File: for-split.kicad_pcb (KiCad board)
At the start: 2 copper layers, 114.3 x 95.3 mm, 84 parts, among them J1 TRRS, J2 TRRS, U1 ProMicro

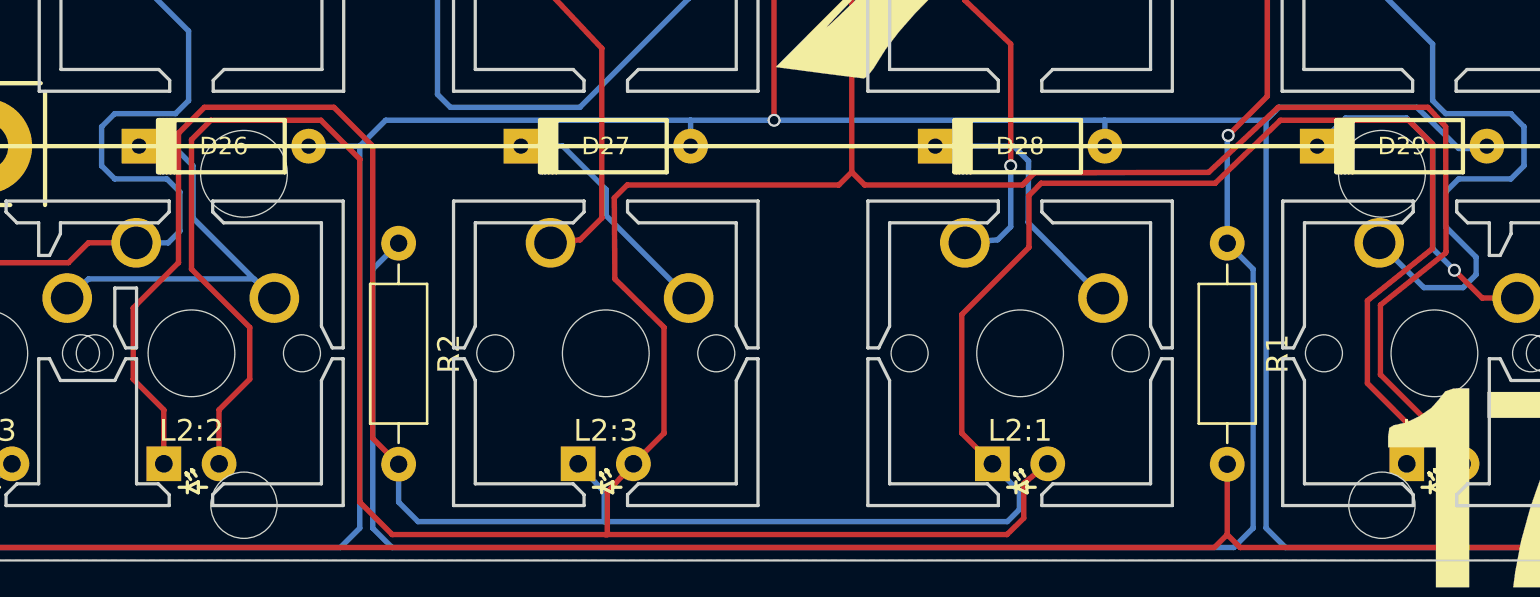
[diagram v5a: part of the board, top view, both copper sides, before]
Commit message: Fix L2.2 cathode trace
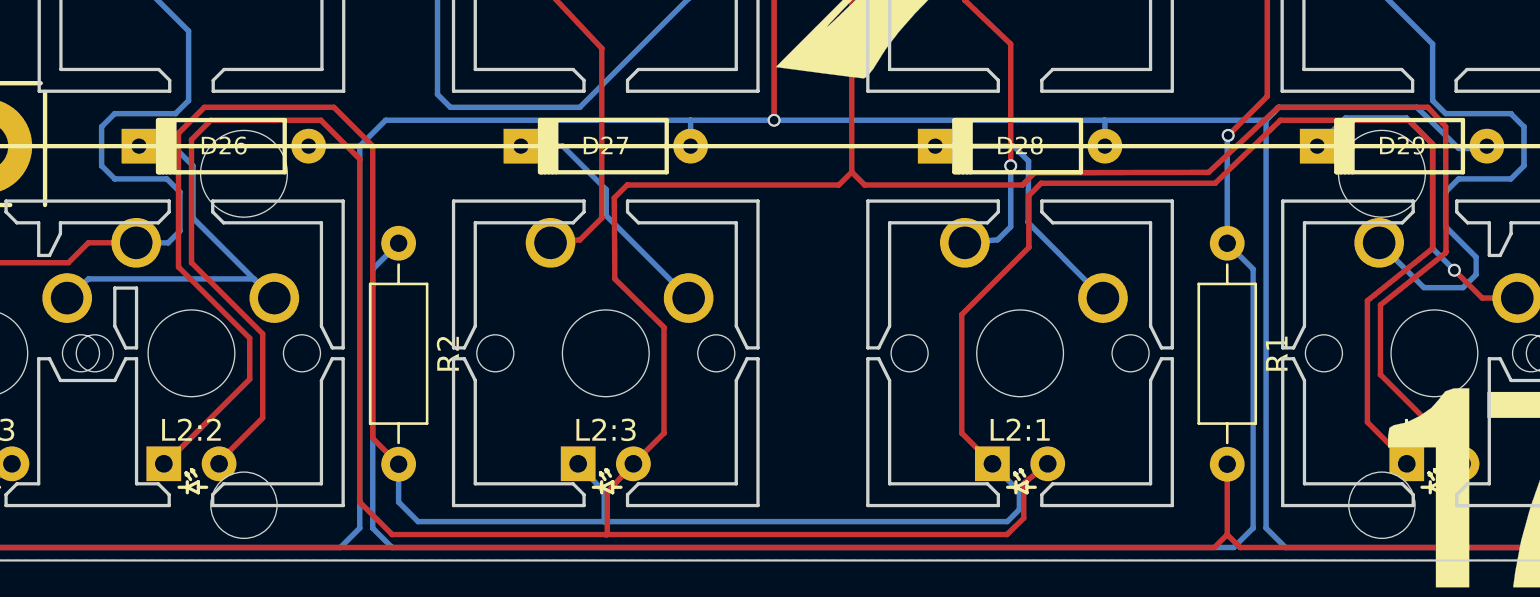
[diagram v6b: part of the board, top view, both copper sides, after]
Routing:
- net Net-(L2:0-Pad1): track 130.1 -> 131.7 mm
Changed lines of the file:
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@@
   (segment (start 154.85191 158.353801) (end 154.77254 158.353801) (width 0.25) (layer F.Cu) (net 54))
   (segment (start 144.959212 158.353801) (end 154.77254 158.353801) (width 0.25) (layer F.Cu) (net 54))
-  (segment (start 137.001829 152.618938) (end 138.410747 151.21002) (width 0.25) (layer F.Cu) (net 54))
-  (segment (start 138.410747 151.21002) (end 138.410747 148.82876) (width 0.25) (layer F.Cu) (net 54))
-  (segment (start 138.410747 148.82876) (end 135.731829 146.149842) (width 0.25) (layer F.Cu) (net 54))
-  (segment (start 135.731829 146.149842) (end 135.731829 140.196692) (width 0.25) (layer F.Cu) (net 54))
+  (segment (start 137.001829 155.000198) (end 139.006062 152.995965) (width 0.25) (layer F.Cu) (net 54))
+  (segment (start 139.006062 152.995965) (end 139.006062 149.126418) (width 0.25) (layer F.Cu) (net 54))
+  (segment (start 139.006062 149.126418) (end 135.731829 145.852185) (width 0.25) (layer F.Cu) (net 54))
+  (segment (start 135.731829 145.852185) (end 135.731829 140.196692) (width 0.25) (layer F.Cu) (net 54))
   (segment (start 135.731829 140.196692) (end 136.624802 139.303719) (width 0.25) (layer F.Cu) (net 54))
   (segment (start 136.624802 139.303719) (end 141.684979 139.303719) (width 0.25) (layer F.Cu) (net 54))
@@
   (segment (start 143.470925 141.089665) (end 143.470925 156.865513) (width 0.25) (layer F.Cu) (net 54))
   (segment (start 143.470925 156.865513) (end 144.959212 158.353801) (width 0.25) (layer F.Cu) (net 54))
-  (segment (start 137.001829 155.09939) (end 137.001829 152.618938) (width 0.25) (layer F.Cu) (net 54) (status 10))
+  (segment (start 137.001829 155.09939) (end 137.001829 155.000198) (width 0.25) (layer F.Cu) (net 54) (status 400010))
   (segment (start 154.77254 158.353801) (end 173.227307 158.353801) (width 0.25) (layer F.Cu) (net 54))
   (segment (start 174 157.6) (end 174 156) (width 0.25) (layer F.Cu) (net 54))
@@
   (segment (start 183.357032 158.353801) (end 183.952347 158.949116) (width 0.25) (layer F.Cu) (net 55))
   (segment (start 183.357032 155.119212) (end 183.357032 158.353801) (width 0.25) (layer F.Cu) (net 55) (status 10))
-  (segment (start 191.612073 155.09939) (end 191.612073 153.214253) (width 0.25) (layer F.Cu) (net 56) (status 10))
+  (segment (start 191.612073 155.09939) (end 191.612073 155.000198) (width 0.25) (layer F.Cu) (net 56) (status 400010))
   (segment (start 171.153074 153.690472) (end 172.561992 155.09939) (width 0.25) (layer F.Cu) (net 56) (status 20))
   (segment (start 171.153074 148.233445) (end 171.153074 153.690472) (width 0.25) (layer F.Cu) (net 56))
@@
   (segment (start 192.8 145.2) (end 192.8 140.4) (width 0.25) (layer F.Cu) (net 56))
   (segment (start 189.8 147.6) (end 192.8 145.2) (width 0.25) (layer F.Cu) (net 56))
-  (segment (start 189.8 151.4) (end 189.8 147.6) (width 0.25) (layer F.Cu) (net 56))
-  (segment (start 191.612073 153.214253) (end 189.8 151.4) (width 0.25) (layer F.Cu) (net 56))
+  (segment (start 189.8 153.185945) (end 189.8 147.6) (width 0.25) (layer F.Cu) (net 56))
+  (segment (start 191.612073 155.000198) (end 189.8 153.185945) (width 0.25) (layer F.Cu) (net 56))
   (segment (start 153.51191 155.09939) (end 154.71191 156.4) (width 0.25) (layer B.Cu) (net 56) (status 10))
   (segment (start 154.71191 156.4) (end 154.71191 157.758486) (width 0.25) (layer B.Cu) (net 56))
@@
   (segment (start 146.149842 157.758486) (end 154.79128 157.758486) (width 0.25) (layer B.Cu) (net 56))
   (segment (start 154.79128 157.758486) (end 173.246047 157.758486) (width 0.25) (layer B.Cu) (net 56))
-  (segment (start 134.461829 155.09939) (end 134.461829 152.618938) (width 0.25) (layer F.Cu) (net 56) (status 10))
-  (segment (start 134.461829 152.618938) (end 133.052911 151.21002) (width 0.25) (layer F.Cu) (net 56))
+  (segment (start 134.461829 155.09939) (end 134.541199 155.079568) (width 0.25) (layer F.Cu) (net 56) (status 400010))
+  (segment (start 134.541199 155.079568) (end 138.410747 151.21002) (width 0.25) (layer F.Cu) (net 56))
   (segment (start 145.25687 156.865514) (end 146.149842 157.758486) (width 0.25) (layer B.Cu) (net 56))
-  (segment (start 133.052911 151.21002) (end 133.052911 147.935788) (width 0.25) (layer F.Cu) (net 56))
-  (segment (start 133.052911 147.935788) (end 135.136514 145.852185) (width 0.25) (layer F.Cu) (net 56))
+  (segment (start 138.410747 151.21002) (end 138.410747 149.326418) (width 0.25) (layer F.Cu) (net 56))
+  (segment (start 138.410747 149.326418) (end 135.136514 146.052184) (width 0.25) (layer F.Cu) (net 56))
   (segment (start 145.25687 155.119212) (end 145.25687 156.865514) (width 0.25) (layer B.Cu) (net 56) (status 10))
   (segment (start 144.06624 153.928582) (end 145.25687 155.119212) (width 0.25) (layer F.Cu) (net 56) (status 20))
@@
   (segment (start 136.327144 138.708404) (end 142.280295 138.708404) (width 0.25) (layer F.Cu) (net 56))
   (segment (start 135.136514 139.899034) (end 136.327144 138.708404) (width 0.25) (layer F.Cu) (net 56))
-  (segment (start 135.136514 145.852185) (end 135.136514 139.899034) (width 0.25) (layer F.Cu) (net 56))
+  (segment (start 135.136514 146.052184) (end 135.136514 139.899034) (width 0.25) (layer F.Cu) (net 56))
   (segment (start 128.427144 76.497983) (end 125.909131 76.497983) (width 0.25) (layer B.Cu) (net 57))
   (segment (start 125.909131 76.497983) (end 125.016158 75.60501) (width 0.25) (layer B.Cu) (net 57))

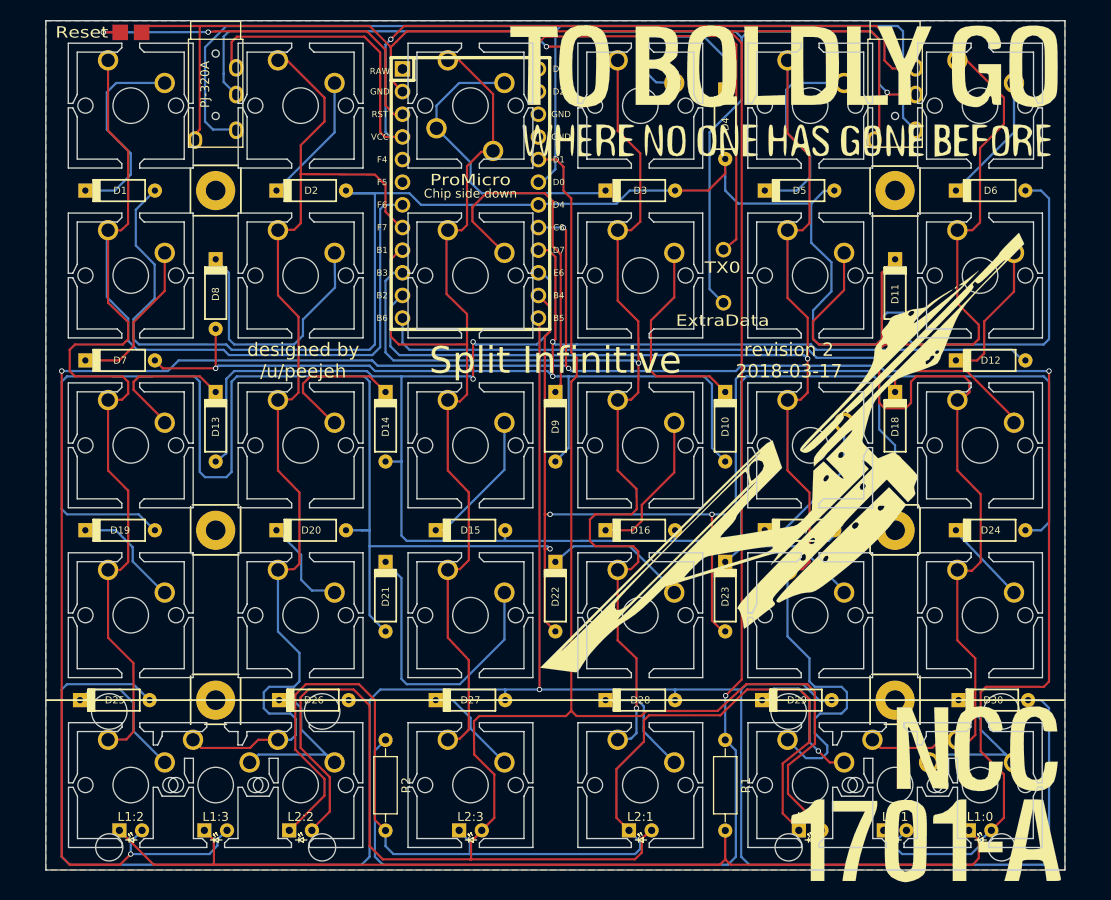
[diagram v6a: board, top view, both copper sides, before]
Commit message: Remove graphics from backside of PCB
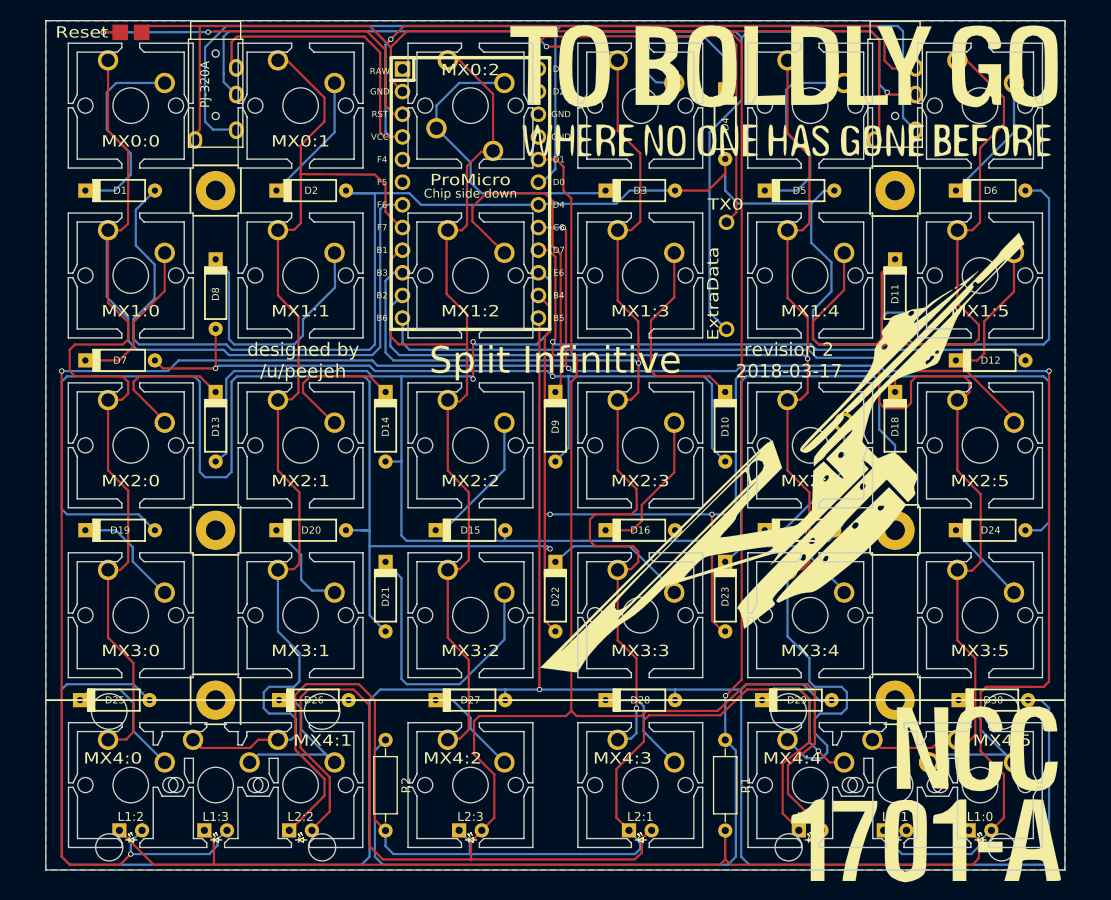
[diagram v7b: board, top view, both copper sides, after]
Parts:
- U1: footprint idle-hands:Pro_Micro -> idle-hands:Pro_Micro_ChipSideDown
- moved TX0 3.09 mm to (183.4, 88.9)
- moved EXTRADATA1 2.99 mm to (183.4, 100.9)
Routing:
- net Net-(TX0-Pad1): track 49.5 -> 46.2 mm
- net Net-(EXTRADATA1-Pad1): track 124.8 -> 127.9 mm

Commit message: Add connectors for rows and columns
Changes have been made to add connectors for the rows and columns so that two PCBs can be bridged together to create a single 12x5 matrix running from a single Pro Micro.
Provision for removal of the bottom row has been removed to make way for the connectors.
Holes for 2U stablizers have been removed to increase PCB stiffness.
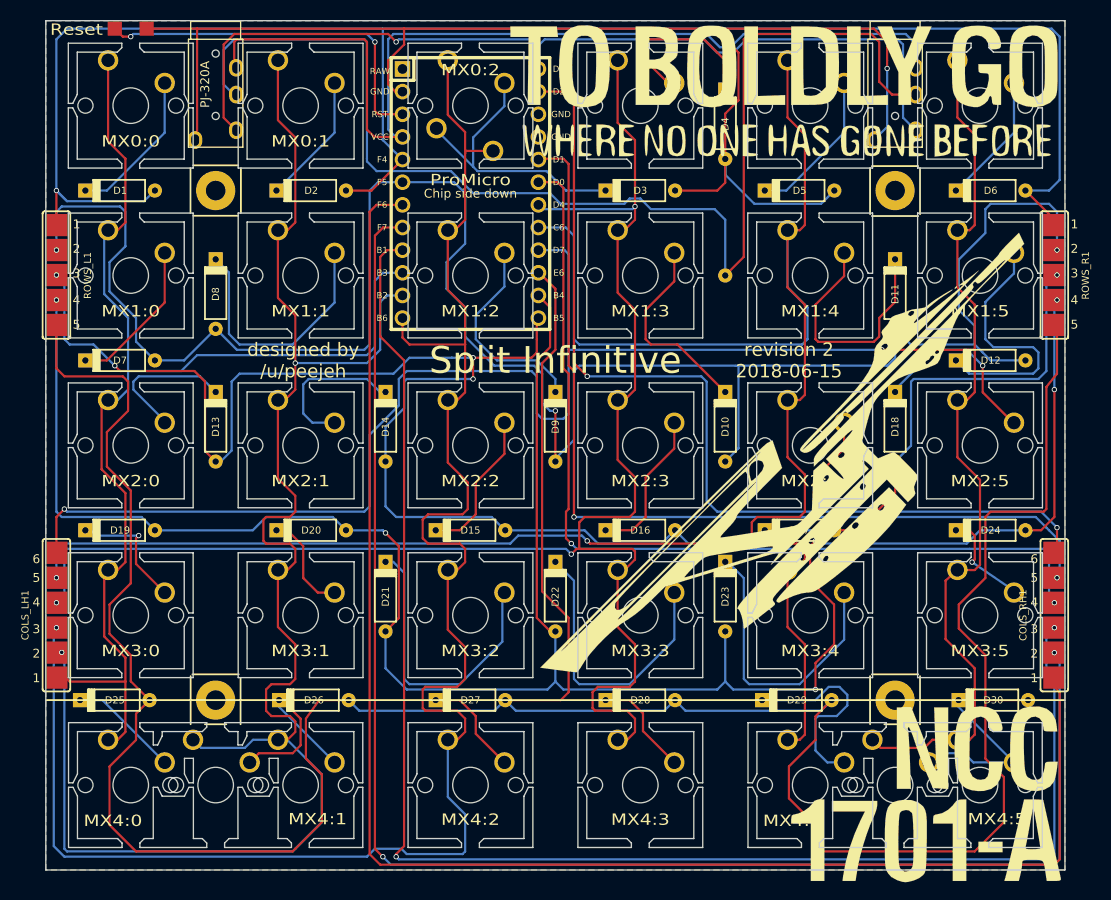
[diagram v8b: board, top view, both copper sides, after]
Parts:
- removed the Hole at (126.2, 121.4)
- removed the Hole at (202.4, 121.4)
- removed L1:0, L1:1, L1:2, L1:3, L2:0, L2:1, L2:2, L2:3: LED, idle-hands:MX_LED
- removed R1, R2: R, Resistors_THT:R_Axial_DIN0207_L6.3mm_D2.5mm_P10.16mm_Horizontal
- removed TX0: TX0, canadian_footprints:SIngle_Pad
- added COLS_LH1: Conn_01x06, idle-hands:CONNECTOR_6, F.Cu at (108.3, 131.0)
- added COLS_RH1: Conn_01x06, idle-hands:CONNECTOR_6, F.Cu at (220.3, 131.0)
- added ROWS_L1: Conn_01x05, idle-hands:CONNECTOR_5, F.Cu at (108.3, 92.9)
- added ROWS_R1: Conn_01x05, idle-hands:CONNECTOR_5, F.Cu at (220.3, 92.9)
- EXTRADATA1: footprint canadian_footprints:SIngle_Pad -> idle-hands:Square_Pad
- GROUND1, RESET1: footprint canadian_footprints:SIngle_Pad -> idle-hands:Single_Pad
- J1: footprint Keebio-Parts:TRRS-PJ-320A -> idle-hands:PJ-320A
- moved EXTRADATA1 8.03 mm to (183.4, 92.9), turned to 90 degrees
- moved GROUND1 2.50 mm to (118.5, 65.2)
- moved RESET1 2.47 mm to (114.9, 65.2)
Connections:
- J1 pad 2: Net-(J1-Pad2) -> /Data
- J2 pad 2: Net-(J1-Pad2) -> /Data
- U1 pad 10: /Col3 -> /Col0
- U1 pad 11: /Col4 -> /Col1
- U1 pad 12: /Col5 -> /Col2
- U1 pad 13: Net-(TX0-Pad1) -> /Data
- U1 pad 14: Net-(U1-Pad14) -> /Col11
- U1 pad 17: /LED2 -> /Col10
- U1 pad 18: Net-(J1-Pad2) -> /Col9
- U1 pad 19: /Row0 -> /Col3
- U1 pad 20: /LED1 -> /Col4
- U1 pad 21: /Row1 -> /Col5
- U1 pad 22: /Row2 -> /Row4
- U1 pad 24: /Row4 -> /Row2
- U1 pad 5: Net-(U1-Pad5) -> /Row0
- U1 pad 6: Net-(U1-Pad6) -> /Row1
- U1 pad 7: /Col0 -> /Col6
- U1 pad 8: /Col1 -> /Col7
- U1 pad 9: /Col2 -> /Col8
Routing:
- net /LED1: track 284.5 -> 0.00 mm, vias 5 -> 0
- net /LED2: track 218.0 -> 0.00 mm
- net /Col6: track 0.00 -> 174.8 mm
- net /Col7: track 0.00 -> 173.4 mm, vias 0 -> 2
- net /Col8: track 0.00 -> 172.1 mm, vias 0 -> 2
- net GND: track 264.1 -> 117.1 mm
- net Net-(L2:0-Pad1): track 131.7 -> 0.00 mm
- net Net-(J1-Pad2): track 121.8 -> 0.00 mm
- net Net-(L1:0-Pad1): track 114.5 -> 0.00 mm
- net /Col11: track 0.00 -> 106.2 mm, vias 0 -> 2
- net /Col10: track 0.00 -> 103.4 mm, vias 0 -> 2
- net /Col9: track 0.00 -> 103.3 mm, vias 0 -> 2
- net /Data: track 0.00 -> 102.8 mm, vias 0 -> 1
- net /Col2: track 110.1 -> 199.9 mm, vias 0 -> 1
- net /Row4: track 255.9 -> 342.2 mm, vias 1 -> 0
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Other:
- board text added: "revision 2 2018-06-15"
- board text removed: "revision 2 2018-03-17"
